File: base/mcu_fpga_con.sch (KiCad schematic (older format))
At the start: 0 parts

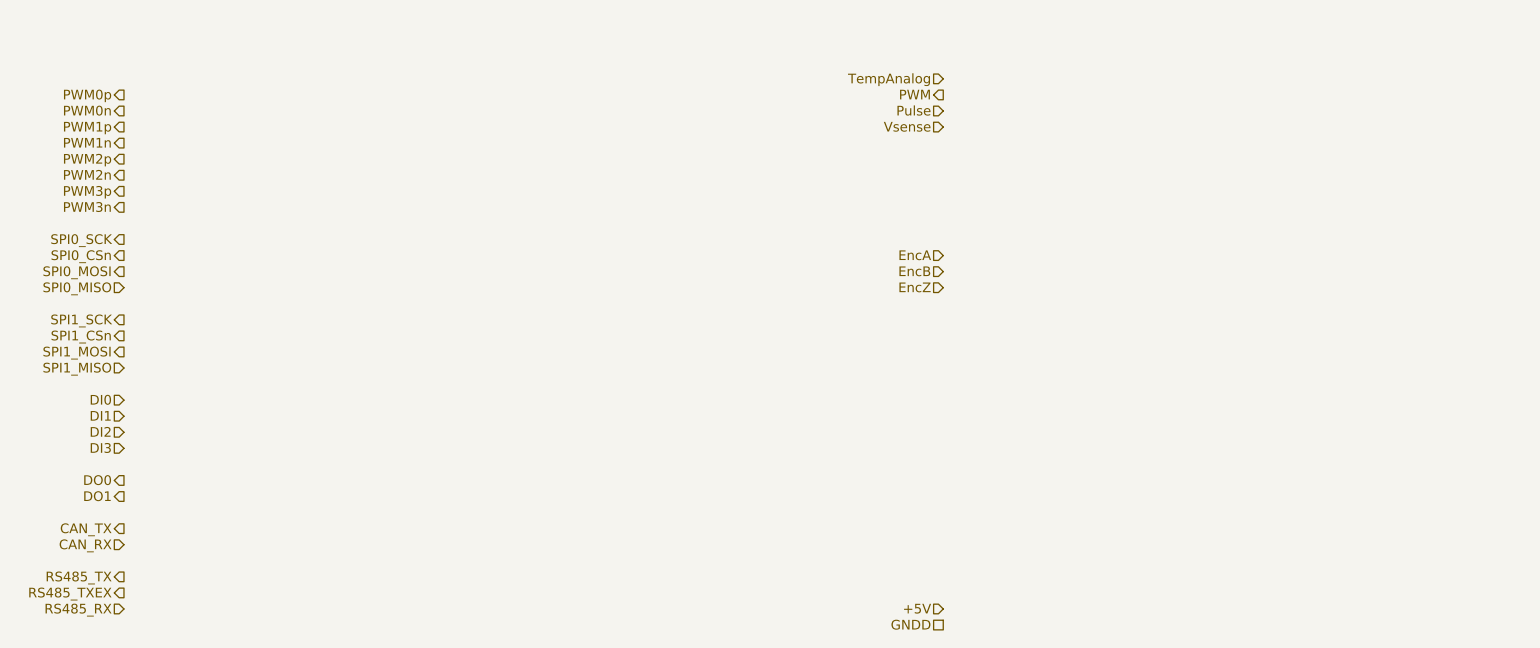
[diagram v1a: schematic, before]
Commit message: 1. Add STM32 pinmux for Core407V. 2. Add 'power' lib. 3. Add interface to Core407V board.
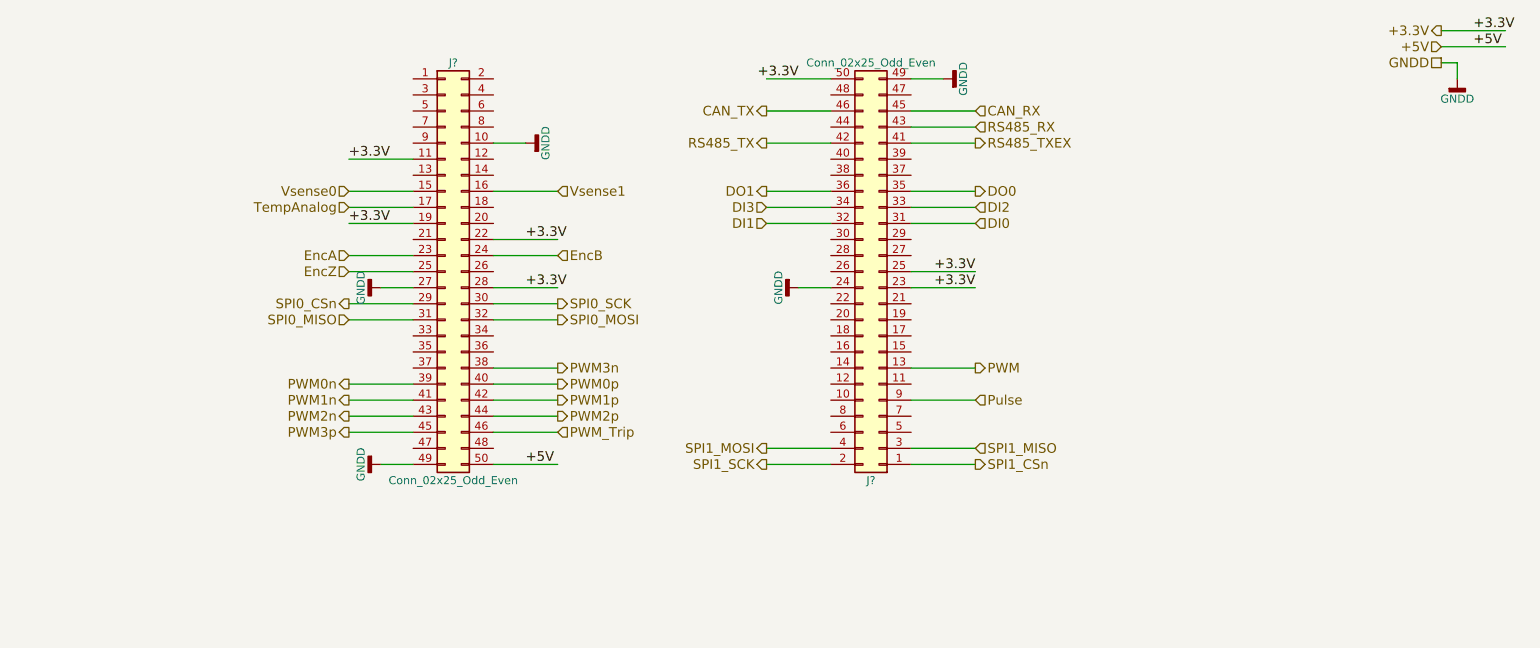
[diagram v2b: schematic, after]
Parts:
- added J? (x2): Conn_02x25_Odd_Even, symbol Conn_02x25_Odd_Even
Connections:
- net labels added: +3.3V, PWM_Trip, Vsense0, Vsense1
- net labels removed: Vsense
- wire segments 0 -> 53

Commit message: draf 0.1 of mosfets_sens_isol.sch
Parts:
- gave numbers to parts that had none: 2
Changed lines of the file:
@@
 LIBS:nxp
 LIBS:Logic_74xx
+LIBS:silabs
 LIBS:4hbd-base-cache
 EELAYER 25 0
@@
 Vsense1
 $Comp
-L Conn_02x25_Odd_Even J?
+L Conn_02x25_Odd_Even J14
 U 1 1 5A2BAF82
 P 4000 2600
-F 0 "J?" H 4050 3900 50  0000 C CNN
+F 0 "J14" H 4050 3900 50  0000 C CNN
 F 1 "Conn_02x25_Odd_Even" H 4050 1300 50  0000 C CNN
 F 2 "" H 4000 2600 50  0001 C CNN
@@
 $EndComp
 $Comp
-L Conn_02x25_Odd_Even J?
+L Conn_02x25_Odd_Even J15
 U 1 1 5A2BB01B
 P 6700 2600
-F 0 "J?" H 6750 3900 50  0000 C CNN
+F 0 "J15" H 6750 3900 50  0000 C CNN
 F 1 "Conn_02x25_Odd_Even" H 6750 1300 50  0000 C CNN
 F 2 "" H 6700 2600 50  0001 C CNN
@@
 	10300 1300 10300 1400
 $Comp
-L GNDD #PWR?
+L GNDD #PWR17
 U 1 1 5A2BBBBD
 P 10300 1400
-F 0 "#PWR?" H 10300 1150 50  0001 C CNN
+F 0 "#PWR17" H 10300 1150 50  0001 C CNN
 F 1 "GNDD" H 10300 1275 50  0000 C CNN
 F 2 "" H 10300 1400 50  0001 C CNN
@@
 	4300 1800 4500 1800
 $Comp
-L GNDD #PWR?
+L GNDD #PWR13
 U 1 1 5A2BBDBA
 P 3600 3800
-F 0 "#PWR?" H 3600 3550 50  0001 C CNN
+F 0 "#PWR13" H 3600 3550 50  0001 C CNN
 F 1 "GNDD" H 3600 3675 50  0000 C CNN
 F 2 "" H 3600 3800 50  0001 C CNN
@@
 $EndComp
 $Comp
-L GNDD #PWR?
+L GNDD #PWR12
 U 1 1 5A2BBDD1
 P 3600 2700
-F 0 "#PWR?" H 3600 2450 50  0001 C CNN
+F 0 "#PWR12" H 3600 2450 50  0001 C CNN
 F 1 "GNDD" H 3600 2575 50  0000 C CNN
 F 2 "" H 3600 2700 50  0001 C CNN
@@
 $EndComp
 $Comp
-L GNDD #PWR?
+L GNDD #PWR14
 U 1 1 5A2BBDE2
 P 4500 1800
-F 0 "#PWR?" H 4500 1550 50  0001 C CNN
+F 0 "#PWR14" H 4500 1550 50  0001 C CNN
 F 1 "GNDD" H 4500 1675 50  0000 C CNN
 F 2 "" H 4500 1800 50  0001 C CNN
@@
 	6900 1400 7100 1400
 $Comp
-L GNDD #PWR?
+L GNDD #PWR16
 U 1 1 5A2BC169
 P 7100 1400
-F 0 "#PWR?" H 7100 1150 50  0001 C CNN
+F 0 "#PWR16" H 7100 1150 50  0001 C CNN
 F 1 "GNDD" H 7100 1275 50  0000 C CNN
 F 2 "" H 7100 1400 50  0001 C CNN
@@
 	6400 2700 6200 2700
 $Comp
-L GNDD #PWR?
+L GNDD #PWR15
 U 1 1 5A2BC182
 P 6200 2700
-F 0 "#PWR?" H 6200 2450 50  0001 C CNN
+F 0 "#PWR15" H 6200 2450 50  0001 C CNN
 F 1 "GNDD" H 6200 2575 50  0000 C CNN
 F 2 "" H 6200 2700 50  0001 C CNN

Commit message: 1. Separate dio_can_rs485 sheet into two: dio + can_rs485. 2. Move can and rs485 into digital power domain 3. Add CAN transiever to can_rs485 sheet
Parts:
- J14, J15: footprint (none) -> Connector_PinHeader_2.54mm:PinHeader_2x25_P2.54mm_Vertical
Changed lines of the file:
@@
 LIBS:dc-dc
 LIBS:regul
+LIBS:interface
+LIBS:ESD_Protection
 LIBS:4hbd-base-cache
 EELAYER 25 0
@@
 $Descr A4 11693 8268
 encoding utf-8
-Sheet 5 8
+Sheet 5 9
 Title ""
 Date ""
@@
 F 0 "J14" H 4050 3900 50  0000 C CNN
 F 1 "Conn_02x25_Odd_Even" H 4050 1300 50  0000 C CNN
-F 2 "" H 4000 2600 50  0001 C CNN
+F 2 "Connector_PinHeader_2.54mm:PinHeader_2x25_P2.54mm_Vertical" H 4000 2600 50  0001 C CNN
 F 3 "" H 4000 2600 50  0001 C CNN
 	1    4000 2600
@@
 F 0 "J15" H 6750 3900 50  0000 C CNN
 F 1 "Conn_02x25_Odd_Even" H 6750 1300 50  0000 C CNN
-F 2 "" H 6700 2600 50  0001 C CNN
+F 2 "Connector_PinHeader_2.54mm:PinHeader_2x25_P2.54mm_Vertical" H 6700 2600 50  0001 C CNN
 F 3 "" H 6700 2600 50  0001 C CNN
 	1    6700 2600

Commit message: Update schematics: 1. Connect analog voltages to MCU board connector 2. Implement Power DC/DC
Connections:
- net labels added: ADC_Csens0, ADC_Csens1
- net labels removed: TempAnalog
- wire segments 53 -> 54
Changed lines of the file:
@@
 EncZ
 Text HLabel 3400 2200 0    60   Input ~ 0
-TempAnalog
+ADC_Csens1
 Text HLabel 7300 3200 2    60   Output ~ 0
 PWM
 Text HLabel 7300 3400 2    60   Input ~ 0
 Pulse
-Text HLabel 4700 2100 2    60   Input ~ 0
+Text HLabel 4700 3100 2    60   Input ~ 0
 Vsense1
 $Comp
@@
 	3800 2200 3400 2200
 Wire Wire Line
-	4700 2100 4300 2100
+	4700 3100 4300 3100
 Text HLabel 3400 2100 0    60   Input ~ 0
+ADC_Csens0
+Wire Wire Line
+	6400 3800 6000 3800
+Wire Wire Line
+	6400 3700 6000 3700
+Wire Wire Line
+	7300 3800 6900 3800
+Wire Wire Line
+	7300 3700 6900 3700
+Wire Wire Line
+	7300 3400 6900 3400
+Wire Wire Line
+	7300 3200 6900 3200
+Wire Wire Line
+	7300 1600 6900 1600
+Wire Wire Line
+	6400 1600 6000 1600
+Wire Wire Line
+	7300 1700 6900 1700
+Wire Wire Line
+	7300 1800 6900 1800
+Wire Wire Line
+	6400 1800 6000 1800
+Wire Wire Line
+	7300 2100 6900 2100
+Wire Wire Line
+	7300 2200 6900 2200
+Wire Wire Line
+	7300 2300 6900 2300
+Wire Wire Line
+	6400 2100 6000 2100
+Wire Wire Line
+	6400 2200 6000 2200
+Wire Wire Line
+	6400 2300 6000 2300
+Text HLabel 4700 3000 2    60   Input ~ 0
 Vsense0
 Wire Wire Line
-	6400 3800 6000 3800
-Wire Wire Line
-	6400 3700 6000 3700
-Wire Wire Line
-	7300 3800 6900 3800
-Wire Wire Line
-	7300 3700 6900 3700
-Wire Wire Line
-	7300 3400 6900 3400
-Wire Wire Line
-	7300 3200 6900 3200
-Wire Wire Line
-	7300 1600 6900 1600
-Wire Wire Line
-	6400 1600 6000 1600
-Wire Wire Line
-	7300 1700 6900 1700
-Wire Wire Line
-	7300 1800 6900 1800
-Wire Wire Line
-	6400 1800 6000 1800
-Wire Wire Line
-	7300 2100 6900 2100
-Wire Wire Line
-	7300 2200 6900 2200
-Wire Wire Line
-	7300 2300 6900 2300
-Wire Wire Line
-	6400 2100 6000 2100
-Wire Wire Line
-	6400 2200 6000 2200
-Wire Wire Line
-	6400 2300 6000 2300
+	4700 3000 4300 3000
 $EndSCHEMATC
